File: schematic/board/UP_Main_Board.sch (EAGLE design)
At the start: 18 parts

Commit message: добавил полигоны на плату и добавил буквы на разъём
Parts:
- removed U$5: GPS, cansat-lib:GPS
- added U$1: GPS_NEO6M, NEON-BLADE-2024:GPS_NEO6M
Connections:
- net 5V: now also U$1.VCC; no longer U$5.UCC
- net GND: now also U$1.GND; no longer U$5.GND
- net GPS_RX: now also U$1.TX; no longer U$5.TX
- net GPS_TX: now also U$1.RX; no longer U$5.RX
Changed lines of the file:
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@@
 <part name="R7" library="rcl" library_urn="urn:adsk.eagle:library:334" deviceset="R-EU_" device="R0603" package3d_urn="urn:adsk.eagle:package:23555/3" value="5K1"/>
 <part name="LED7" library="led" library_urn="urn:adsk.eagle:library:259" deviceset="LED" device="SML0603" package3d_urn="urn:adsk.eagle:package:15832/1"/>
-<part name="U$5" library="cansat-lib" deviceset="GPS" device=""/>
 <part name="U$6" library="NEON-BLADE-2024" deviceset="PBS_SMD_X9" device=""/>
 <part name="U$7" library="NEON-BLADE-2024" deviceset="PBS_SMD_X9" device=""/>
@@
 <part name="R4" library="rcl" library_urn="urn:adsk.eagle:library:334" deviceset="R-EU_" device="R0603" package3d_urn="urn:adsk.eagle:package:23555/3" value="2k"/>
 <part name="JP1" library="pinhead" library_urn="urn:adsk.eagle:library:325" deviceset="PINHD-1X2" device="" package3d_urn="urn:adsk.eagle:package:22435/2"/>
+<part name="U$1" library="NEON-BLADE-2024" deviceset="GPS_NEO6M" device=""/>
 </parts>
 <sheets>
@@
 <attribute name="VALUE" x="34.925" y="37.592" size="1.778" layer="96" rot="R270"/>
 </instance>
-<instance part="U$5" gate="G$1" x="228.6" y="129.54" smashed="yes">
-<attribute name="NAME" x="220.98" y="142.24" size="1.27" layer="95"/>
-</instance>
 <instance part="U$6" gate="G$1" x="134.62" y="-5.08" smashed="yes">
 <attribute name="NAME" x="128.27" y="8.255" size="1.778" layer="95"/>
@@
 <attribute name="VALUE" x="19.05" y="137.16" size="1.778" layer="96"/>
 </instance>
+<instance part="U$1" gate="G$1" x="226.06" y="129.54" smashed="yes"/>
 </instances>
 <busses>
@@
 </segment>
 <segment>
-<pinref part="U$5" gate="G$1" pin="GND"/>
-<wire x1="215.9" y1="137.16" x2="205.74" y2="137.16" width="0.1524" layer="91"/>
-<label x="205.74" y="137.16" size="1.778" layer="95"/>
-</segment>
-<segment>
 <wire x1="104.14" y1="-20.32" x2="86.36" y2="-20.32" width="0.1524" layer="91"/>
 <label x="86.36" y="-20.32" size="1.778" layer="95"/>
 <pinref part="U$8" gate="G$1" pin="6"/>
 </segment>
+<segment>
+<pinref part="U$1" gate="G$1" pin="GND"/>
+<wire x1="220.06" y1="133.54" x2="213.36" y2="133.54" width="0.1524" layer="91"/>
+<label x="213.36" y="134.62" size="1.778" layer="95"/>
+</segment>
 </net>
 <net name="3V3" class="0">
@@
 </segment>
 <segment>
-<pinref part="U$5" gate="G$1" pin="UCC"/>
-<wire x1="215.9" y1="121.92" x2="205.74" y2="121.92" width="0.1524" layer="91"/>
-<label x="205.74" y="121.92" size="1.778" layer="95"/>
-</segment>
-<segment>
 <wire x1="132.08" y1="-25.4" x2="116.84" y2="-25.4" width="0.1524" layer="91"/>
 <label x="116.84" y="-25.4" size="1.778" layer="95"/>
 <pinref part="U$7" gate="G$1" pin="1"/>
+</segment>
+<segment>
+<pinref part="U$1" gate="G$1" pin="VCC"/>
+<wire x1="220.06" y1="124.54" x2="220.06" y2="124.46" width="0.1524" layer="91"/>
+<wire x1="220.06" y1="124.46" x2="213.36" y2="124.46" width="0.1524" layer="91"/>
+<label x="210.82" y="124.46" size="1.778" layer="95"/>
 </segment>
 </net>
@@
 </segment>
 <segment>
-<pinref part="U$5" gate="G$1" pin="RX"/>
-<wire x1="215.9" y1="127" x2="205.74" y2="127" width="0.1524" layer="91"/>
-<label x="205.74" y="127" size="1.778" layer="95"/>
+<pinref part="U$1" gate="G$1" pin="RX"/>
+<wire x1="220.06" y1="127.54" x2="213.36" y2="127.54" width="0.1524" layer="91"/>
+<label x="210.82" y="127" size="1.778" layer="95"/>
 </segment>
 </net>
@@
 </segment>
 <segment>
-<pinref part="U$5" gate="G$1" pin="TX"/>
-<wire x1="215.9" y1="132.08" x2="205.74" y2="132.08" width="0.1524" layer="91"/>
-<label x="205.74" y="132.08" size="1.778" layer="95"/>
-</segment>
-</net>
+<pinref part="U$1" gate="G$1" pin="TX"/>
+<wire x1="220.06" y1="130.54" x2="213.36" y2="130.54" width="0.1524" layer="91"/>
+<label x="210.82" y="129.54" size="1.778" layer="95"/>
+</segment>
+</net>

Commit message: забыли моторчик...
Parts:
- removed JP1, JP4: (no value), pinhead:PINHD-1X2
- added R1, R2: 10k, rcl:R-EU_R0603
- added R3, R5: 100, rcl:R-EU_R0603
- added U$3: IRF7905PBF, NEON-BLADE-2024:IRF7905PBF
- added X1, X2, X3, X4: JST-2-K-S, NEON-BLADE-2024:JST-2-K-S
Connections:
- removed net N$37: JP1.2, R4.2
- new net DRUGATEL: R5.1, U$2.PC14
- new net N$2: U$3.D1, X3.1
- new net N$3: R2.1, R5.2, U$3.G1
- new net N$5: R1.2, R3.2, U$3.G2
- new net N$6: R4.2, X2.2
- new net N$8: U$3.D2, X4.1
- new net PERESHIGATEL: R3.1, U$2.PB12
- net 3V3: now also X2.1; no longer JP1.1
- net 5V: now also X3.2
- net CS_LIS: now also U$2.PA4; no longer U$2.PC14
- net GND: now also R1.1, R2.2, U$3.S1, U$3.S2, X1.2; no longer JP4.2
- net N$1: now also X1.1, X4.2; no longer JP4.1
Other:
- moved on the sheet: R4

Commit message: забыи отладочные пины...
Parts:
- added JP1: (no value), pinhead:PINHD-1X4/90
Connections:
- removed net TDC_INT: U$6.7
- removed net USIL_ON: U$2.PA0, U$6.1
- new net APD_FB_VOLT: U$2.PA3, U$6.8
- new net APD_PWM: U$2.PA2, U$6.9
- new net DBG_3V3: JP1.4, U$2.DBG_3V3
- new net SWC: JP1.2, U$2.SWC
- new net SWD: JP1.3, U$2.SWD
- net GND: now also JP1.1, U$2.DBG_GND
- net PHOTORES: now also U$2.PB8
- net STATE: now also U$2.PC15
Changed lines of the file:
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@@
 <part name="R3" library="rcl" library_urn="urn:adsk.eagle:library:334" deviceset="R-EU_" device="R0603" package3d_urn="urn:adsk.eagle:package:23555/3" value="100"/>
 <part name="R5" library="rcl" library_urn="urn:adsk.eagle:library:334" deviceset="R-EU_" device="R0603" package3d_urn="urn:adsk.eagle:package:23555/3" value="100"/>
+<part name="JP1" library="pinhead" library_urn="urn:adsk.eagle:library:325" deviceset="PINHD-1X4" device="/90" package3d_urn="urn:adsk.eagle:package:22404/2"/>
 </parts>
 <sheets>
@@
 <attribute name="VALUE" x="-13.97" y="72.898" size="1.778" layer="96"/>
 </instance>
+<instance part="JP1" gate="A" x="152.4" y="2.54" smashed="yes" rot="R180">
+<attribute name="NAME" x="158.75" y="-5.715" size="1.778" layer="95" rot="R180"/>
+<attribute name="VALUE" x="158.75" y="10.16" size="1.778" layer="96" rot="R180"/>
+</instance>
 </instances>
 <busses>
@@
 <wire x1="76.2" y1="20.32" x2="66.04" y2="20.32" width="0.1524" layer="91"/>
 <label x="68.58" y="20.32" size="1.778" layer="95"/>
+</segment>
+<segment>
+<pinref part="U$2" gate="G$1" pin="DBG_GND"/>
+<wire x1="86.36" y1="81.28" x2="86.36" y2="73.66" width="0.1524" layer="91"/>
+<label x="86.36" y="71.12" size="1.778" layer="95" rot="R90"/>
+</segment>
+<segment>
+<wire x1="154.94" y1="-2.54" x2="167.64" y2="-2.54" width="0.1524" layer="91"/>
+<pinref part="JP1" gate="A" pin="1"/>
+<label x="160.02" y="-2.54" size="1.778" layer="95"/>
 </segment>
 </net>
@@
 <pinref part="R17" gate="G$1" pin="2"/>
 </segment>
+<segment>
+<pinref part="U$2" gate="G$1" pin="PB8"/>
+<wire x1="63.5" y1="109.22" x2="53.34" y2="109.22" width="0.1524" layer="91"/>
+<label x="48.26" y="109.22" size="1.778" layer="95"/>
+</segment>
 </net>
 <net name="STATE" class="0">
@@
 <pinref part="LED8" gate="G$1" pin="A"/>
 </segment>
+<segment>
+<pinref part="U$2" gate="G$1" pin="PC15"/>
+<wire x1="93.98" y1="106.68" x2="104.14" y2="106.68" width="0.1524" layer="91"/>
+<label x="96.52" y="106.68" size="1.778" layer="95"/>
+</segment>
 </net>
 <net name="N$10" class="0">
@@
 <pinref part="LED7" gate="G$1" pin="C"/>
 <pinref part="R7" gate="G$1" pin="1"/>
-</segment>
-</net>
-<net name="USIL_ON" class="0">
-<segment>
-<wire x1="132.08" y1="5.08" x2="114.3" y2="5.08" width="0.1524" layer="91"/>
-<label x="114.3" y="5.08" size="1.778" layer="95"/>
-<pinref part="U$6" gate="G$1" pin="1"/>
-</segment>
-<segment>
-<pinref part="U$2" gate="G$1" pin="PA0"/>
-<wire x1="93.98" y1="111.76" x2="104.14" y2="111.76" width="0.1524" layer="91"/>
-<label x="96.52" y="111.76" size="1.778" layer="95"/>
-</segment>
-</net>
-<net name="TDC_INT" class="0">
-<segment>
-<wire x1="132.08" y1="-10.16" x2="114.3" y2="-10.16" width="0.1524" layer="91"/>
-<label x="114.3" y="-10.16" size="1.778" layer="95"/>
-<pinref part="U$6" gate="G$1" pin="7"/>
 </segment>
 </net>
@@
 </segment>
 </net>
+<net name="APD_FB_VOLT" class="0">
+<segment>
+<pinref part="U$6" gate="G$1" pin="8"/>
+<wire x1="132.08" y1="-12.7" x2="114.3" y2="-12.7" width="0.1524" layer="91"/>
+<label x="111.76" y="-12.7" size="1.778" layer="95"/>
+</segment>
+<segment>
+<pinref part="U$2" gate="G$1" pin="PA3"/>
+<wire x1="93.98" y1="119.38" x2="104.14" y2="119.38" width="0.1524" layer="91"/>
+<label x="96.52" y="119.38" size="1.778" layer="95"/>
+</segment>
+</net>
+<net name="APD_PWM" class="0">
+<segment>
+<pinref part="U$6" gate="G$1" pin="9"/>
+<wire x1="132.08" y1="-15.24" x2="114.3" y2="-15.24" width="0.1524" layer="91"/>
+<label x="111.76" y="-15.24" size="1.778" layer="95"/>
+</segment>
+<segment>
+<pinref part="U$2" gate="G$1" pin="PA2"/>
+<wire x1="93.98" y1="116.84" x2="104.14" y2="116.84" width="0.1524" layer="91"/>
+<label x="96.52" y="116.84" size="1.778" layer="95"/>
+</segment>
+</net>
+<net name="DBG_3V3" class="0">
+<segment>
+<wire x1="154.94" y1="5.08" x2="167.64" y2="5.08" width="0.1524" layer="91"/>
+<pinref part="JP1" gate="A" pin="4"/>
+<label x="160.02" y="5.08" size="1.778" layer="95"/>
+</segment>
+<segment>
+<pinref part="U$2" gate="G$1" pin="DBG_3V3"/>
+<wire x1="71.12" y1="81.28" x2="71.12" y2="73.66" width="0.1524" layer="91"/>
+<label x="71.12" y="68.58" size="1.778" layer="95" rot="R90"/>
+</segment>
+</net>
+<net name="SWD" class="0">
+<segment>
+<wire x1="154.94" y1="2.54" x2="167.64" y2="2.54" width="0.1524" layer="91"/>
+<pinref part="JP1" gate="A" pin="3"/>
+<label x="160.02" y="2.54" size="1.778" layer="95"/>
+</segment>
+<segment>
+<pinref part="U$2" gate="G$1" pin="SWD"/>
+<wire x1="76.2" y1="81.28" x2="76.2" y2="73.66" width="0.1524" layer="91"/>
+<label x="73.66" y="76.2" size="1.778" layer="95" rot="R270"/>
+</segment>
+</net>
+<net name="SWC" class="0">
+<segment>
+<wire x1="154.94" y1="0" x2="167.64" y2="0" width="0.1524" layer="91"/>
+<pinref part="JP1" gate="A" pin="2"/>
+<label x="160.02" y="0" size="1.778" layer="95"/>
+</segment>
+<segment>
+<pinref part="U$2" gate="G$1" pin="SWC"/>
+<wire x1="81.28" y1="81.28" x2="81.28" y2="73.66" width="0.1524" layer="91"/>
+<label x="81.28" y="71.12" size="1.778" layer="95" rot="R90"/>
+</segment>
+</net>

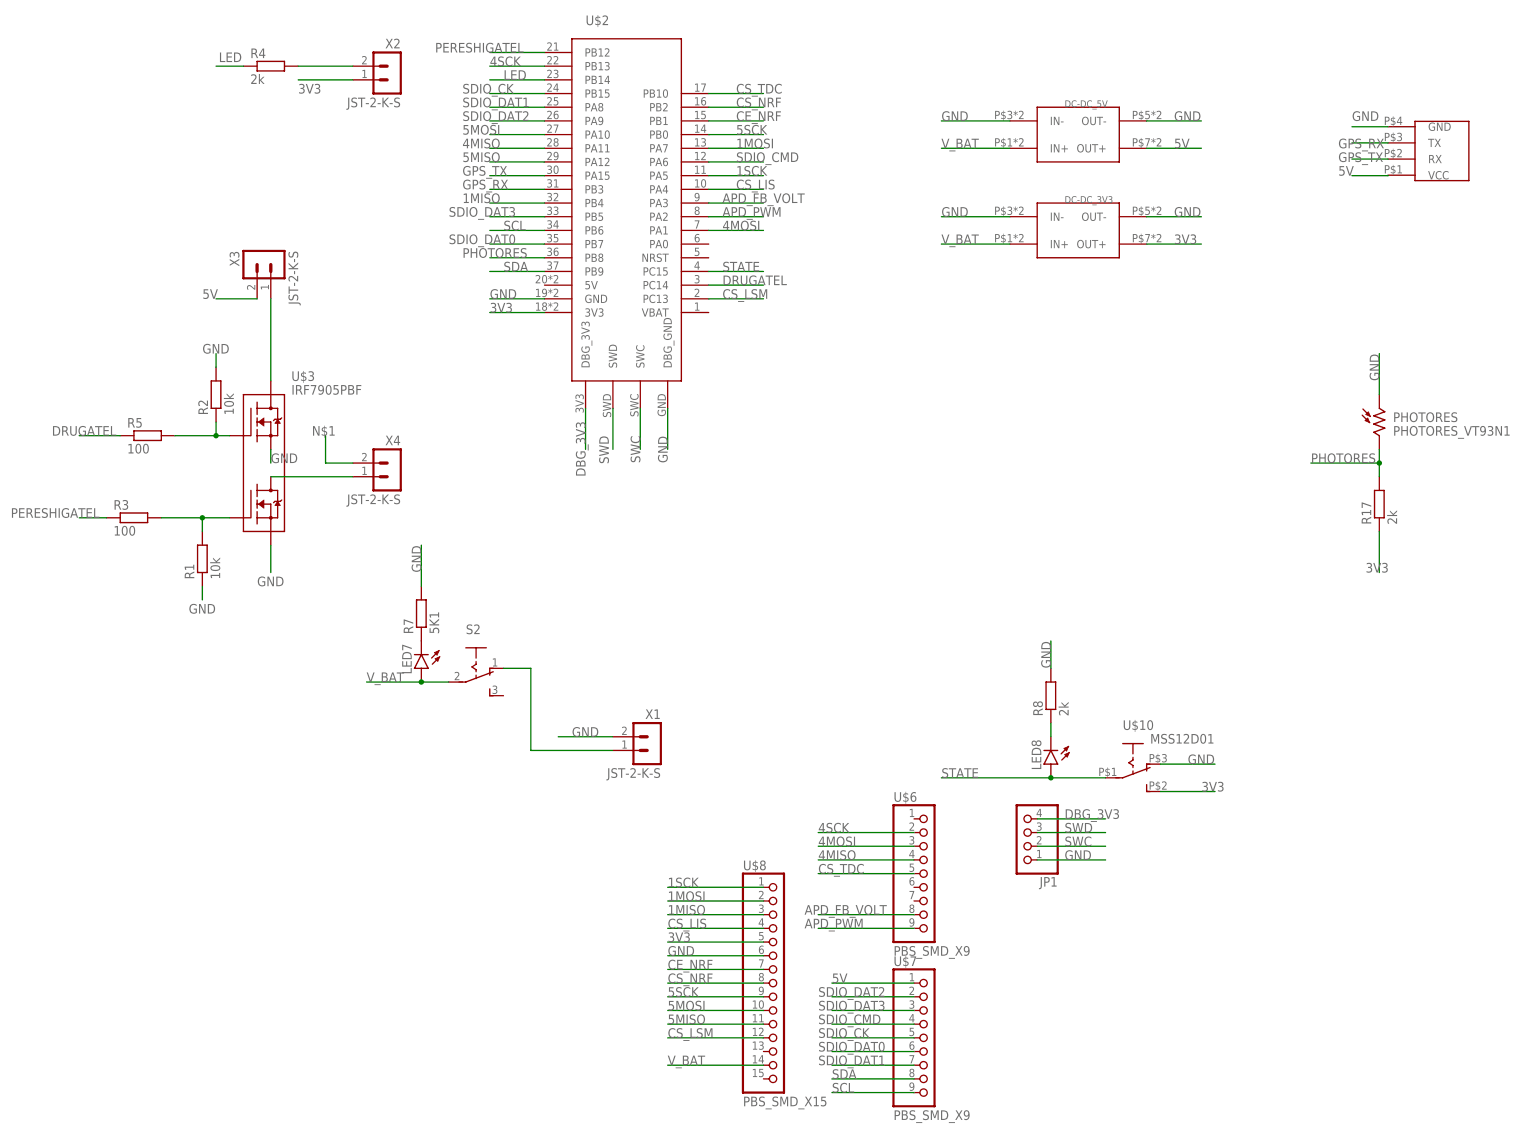
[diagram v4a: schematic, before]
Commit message: Проверил плату верхнюю. Осталось только убрать у GPS отверстие под антенну, чтобы оно не мешало полигону земли
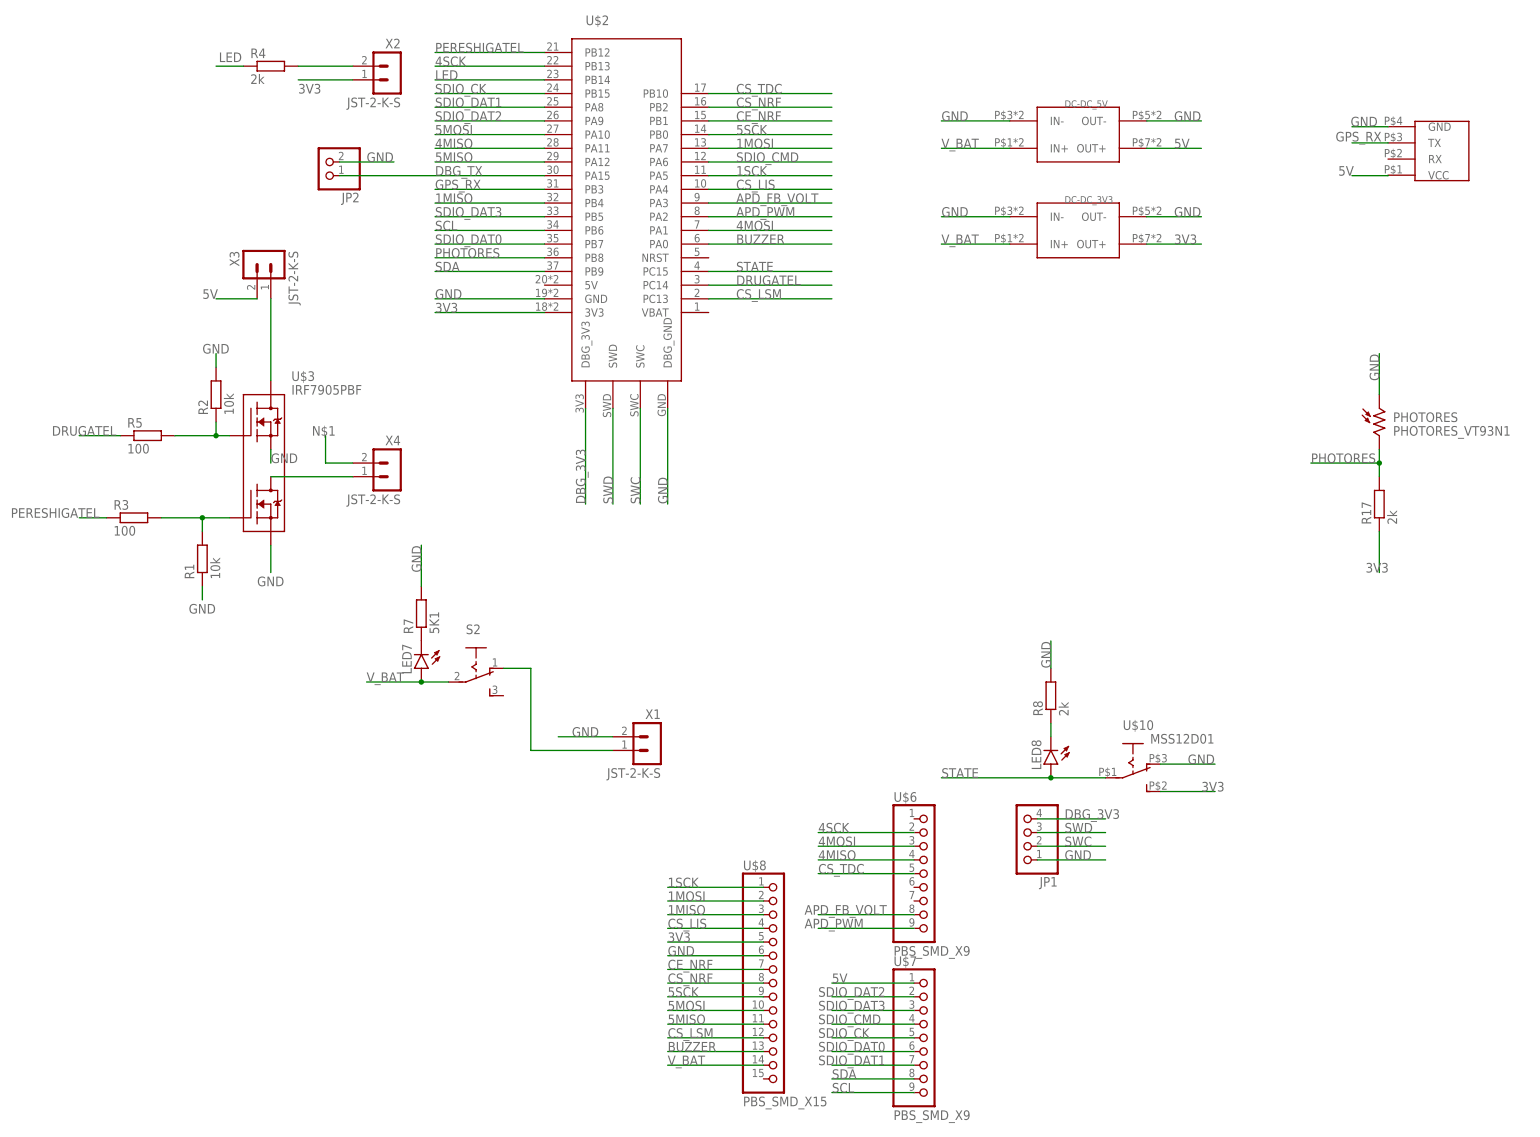
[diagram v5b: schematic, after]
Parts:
- added JP2: (no value), pinhead:PINHD-1X2
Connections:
- removed net GPS_TX: U$1.RX, U$2.PA15
- new net BUZZER: U$2.PA0, U$8.13
- new net DBG_TX: JP2.1, U$2.PA15
- net GND: now also JP2.2
